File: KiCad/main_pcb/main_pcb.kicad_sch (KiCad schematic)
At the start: 11 parts

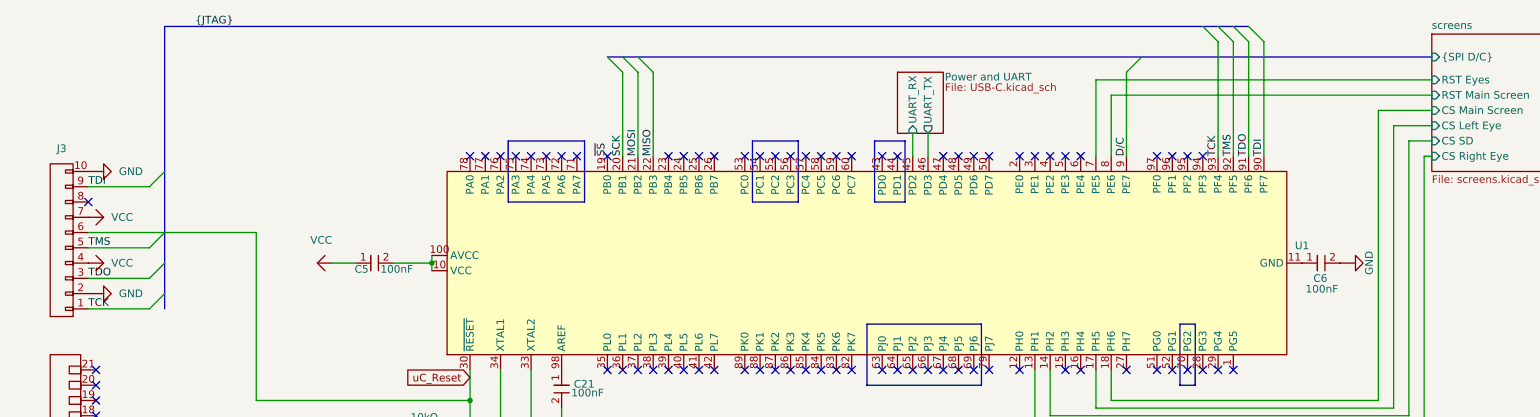
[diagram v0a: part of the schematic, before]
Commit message: feat(KiCad): Adds parallel condensators for USB-C VBUS pin
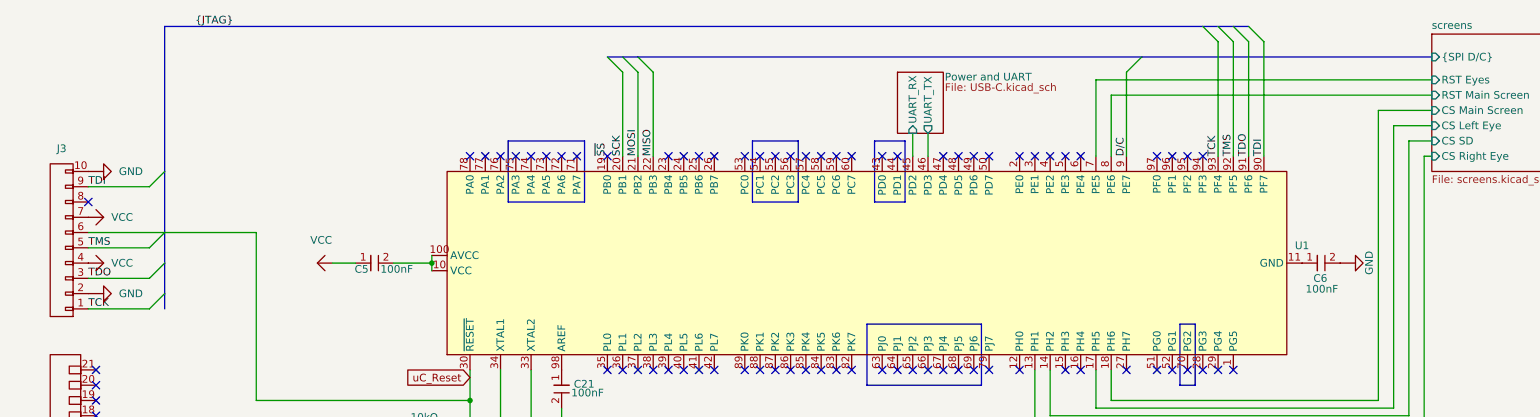
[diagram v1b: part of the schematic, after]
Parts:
- J1, J3, S2, U1, Y1: value (none) -> ~

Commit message: feat(KiCad): Fixes symbols and ERC
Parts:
- C21, C3, C4, C5, C6: symbol lilys_pad:Capacitor -> Lily's Pad:Capacitor
- J1: symbol lilys_pad:Header_21 -> Lily's Pad:Header_21
- J3: symbol lilys_pad:2X5_Header -> Lily's Pad:2X5_Header
- R1: symbol lilys_pad:Resistor -> Lily's Pad:Resistor
- S2: symbol lilys_pad:Push-button_Switch -> Lily's Pad:Push-button_Switch
- U1: symbol lilys_pad:ATmega_2560 -> Lily's Pad:ATmega_2560
- Y1: symbol lilys_pad:Crystal -> Lily's Pad:Crystal
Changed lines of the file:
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@@
 		(company "Lily's Pad")
 	)
+	(bus_alias "JTAG"
+		(members "TDI" "TMS" "TDO" "TCK")
+	)
+	(bus_alias "SPI"
+		(members "SCK" "MOSI" "MISO")
+	)
 	(rectangle
 		(start 96.52 40.6401)
@@
 	(wire
 		(pts
+			(xy 16.51 190.5) (xy 16.51 191.77)
+		)
+		(stroke
+			(width 0)
+			(type default)
+		)
+	)
+	(wire
+		(pts
 			(xy 246.38 86.36) (xy 186.69 86.36)
 		)
@@
 		)
 	)
+	(label "{SPI D{slash}C}"
+		(at 137.16 26.67 0)
+		(effects
+			(font
+				(size 1.27 1.27)
+			)
+			(justify left bottom)
+		)
+	)
 	(label "TMS"
 		(at 217.17 43.18 90)
@@
 	)
 	(symbol
-		(lib_id "lilys_pad:Capacitor")
+		(lib_id "Lily's Pad:Capacitor")
 		(at 232.41 60.96 90)
 		(unit 1)
@@
 	)
 	(symbol
-		(lib_id "lilys_pad:Capacitor")
+		(lib_id "Lily's Pad:Capacitor")
 		(at 100.33 101.6 0)
 		(unit 1)
@@
 	)
 	(symbol
-		(lib_id "lilys_pad:2X5_Header")
+		(lib_id "Lily's Pad:2X5_Header")
 		(at 22.86 57.15 180)
 		(unit 1)
@@
 		(fields_autoplaced yes)
 		(property "Reference" "J3"
-			(at 22.225 41.91 0)
+			(at 22.225 39.37 0)
 			(effects
 				(font
@@
 		)
 		(property "Value" "~"
-			(at 22.86 57.15 0)
+			(at 22.225 41.91 0)
 			(effects
 				(font
@@
 	)
 	(symbol
-		(lib_id "lilys_pad:PWR_FLG")
+		(lib_id "Lily's Pad:PWR_FLG")
 		(at 22.86 194.31 0)
 		(unit 1)
@@
 	)
 	(symbol
-		(lib_id "lilys_pad:VCC")
+		(lib_id "Lily's Pad:VCC")
 		(at 29.21 60.96 90)
 		(unit 1)
@@
 	)
 	(symbol
-		(lib_id "lilys_pad:GND")
+		(lib_id "Lily's Pad:GND")
 		(at 29.21 45.72 90)
 		(unit 1)
@@
 	)
 	(symbol
-		(lib_id "lilys_pad:Resistor")
+		(lib_id "Lily's Pad:Resistor")
 		(at 82.55 88.9 90)
 		(unit 1)
@@
 	)
 	(symbol
-		(lib_id "lilys_pad:VCC")
+		(lib_id "Lily's Pad:VCC")
 		(at 29.21 53.34 90)
 		(unit 1)
@@
 	)
 	(symbol
-		(lib_id "lilys_pad:Capacitor")
+		(lib_id "Lily's Pad:Capacitor")
 		(at 74.93 60.96 90)
 		(unit 1)
@@
 	)
 	(symbol
-		(lib_id "lilys_pad:Crystal")
+		(lib_id "Lily's Pad:Crystal")
 		(at 95.25 100.33 0)
 		(unit 1)
@@
 	)
 	(symbol
-		(lib_id "lilys_pad:VCC")
+		(lib_id "Lily's Pad:VCC")
 		(at 74.93 88.9 270)
 		(unit 1)
@@
 	)
 	(symbol
-		(lib_id "lilys_pad:Push-button_Switch")
+		(lib_id "Lily's Pad:Push-button_Switch")
 		(at 82.55 95.25 270)
 		(unit 1)
@@
 	)
 	(symbol
-		(lib_id "lilys_pad:GND")
+		(lib_id "Lily's Pad:GND")
 		(at 72.39 95.25 270)
 		(unit 1)
@@
 	)
 	(symbol
-		(lib_id "lilys_pad:ATmega_2560")
+		(lib_id "Lily's Pad:ATmega_2560")
 		(at 156.21 60.96 90)
 		(unit 1)
@@
 		(fields_autoplaced yes)
 		(property "Reference" "U1"
-			(at 228.6 58.0546 90)
+			(at 228.6 55.5146 90)
 			(effects
 				(font
@@
 		)
 		(property "Value" "~"
-			(at 156.21 60.96 0)
+			(at 228.6 58.0546 90)
 			(effects
 				(font
@@
 	)
 	(symbol
-		(lib_id "lilys_pad:GND")
+		(lib_id "Lily's Pad:GND")
 		(at 22.86 189.23 180)
 		(unit 1)
@@
 	)
 	(symbol
-		(lib_id "lilys_pad:Capacitor")
+		(lib_id "Lily's Pad:Capacitor")
 		(at 95.25 92.71 0)
 		(unit 1)
@@
 	)
 	(symbol
-		(lib_id "lilys_pad:VCC")
-		(at 16.51 189.23 180)
+		(lib_id "Lily's Pad:VCC")
+		(at 16.51 187.96 180)
 		(unit 1)
 		(exclude_from_sim no)
@@
 		(dnp no)
 		(property "Reference" "#PWR07"
-			(at 16.51 187.96 0)
+			(at 16.51 186.69 0)
 			(effects
 				(font
@@
 		)
 		(property "Value" "VCC"
-			(at 14.732 188.214 0)
+			(at 14.732 186.944 0)
 			(effects
 				(font
@@
 		)
 		(property "Footprint" ""
-			(at 16.51 189.23 0)
+			(at 16.51 187.96 0)
 			(effects
 				(font
@@
 		)
 		(property "Datasheet" ""
-			(at 16.51 189.23 0)
+			(at 16.51 187.96 0)
 			(effects
 				(font
@@
 		)
 		(property "Description" ""
-			(at 16.51 189.23 0)
+			(at 16.51 187.96 0)
 			(effects
 				(font
@@
 	)
 	(symbol
-		(lib_id "lilys_pad:Capacitor")
+		(lib_id "Lily's Pad:Capacitor")
 		(at 105.41 82.55 0)
 		(unit 1)
@@
 	)
 	(symbol
-		(lib_id "lilys_pad:GND")
+		(lib_id "Lily's Pad:GND")
 		(at 29.21 66.04 90)
 		(unit 1)
@@
 	)
 	(symbol
-		(lib_id "lilys_pad:GND")
+		(lib_id "Lily's Pad:GND")
 		(at 105.41 91.44 0)
 		(unit 1)
@@
 		)
 		(property "Value" "GND"
-			(at 107.95 92.0749 0)
+			(at 105.41 95.25 0)
 			(effects
 				(font
 					(size 1.27 1.27)
 				)
-				(justify left)
 			)
 		)
@@
 	)
 	(symbol
-		(lib_id "lilys_pad:PWR_FLG")
+		(lib_id "Lily's Pad:PWR_FLG")
 		(at 29.21 194.31 0)
 		(unit 1)
@@
 	)
 	(symbol
-		(lib_id "lilys_pad:GND")
+		(lib_id "Lily's Pad:GND")
 		(at 237.49 60.96 90)
 		(unit 1)
@@
 	)
 	(symbol
-		(lib_id "lilys_pad:Header_21")
+		(lib_id "Lily's Pad:Header_21")
 		(at 22.86 104.14 180)
 		(unit 1)
@@
 	)
 	(symbol
-		(lib_id "lilys_pad:PWR_FLG")
+		(lib_id "Lily's Pad:PWR_FLG")
 		(at 16.51 194.31 0)
 		(unit 1)
@@
 	)
 	(symbol
-		(lib_id "lilys_pad:VCC")
+		(lib_id "Lily's Pad:VCC")
 		(at 64.77 60.96 270)
 		(unit 1)
@@
 		)
 		(property "Value" "VCC"
-			(at 65.405 57.15 90)
+			(at 63.5 60.9599 90)
 			(effects
 				(font
 					(size 1.27 1.27)
 				)
+				(justify right)
 			)
 		)

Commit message: feat(KiCad): Adds SPI header for bootloader flashing
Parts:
- added J4: 2X4 Header, symbol Lily's Pad:2x4 Header
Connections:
- net MISO: now also J4.3
- net MOSI: now also J4.2
- net SCK: now also J4.1
- new net SS: J4.4
- no-connect marks 92 -> 96
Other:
- moved on the sheet: C21, C3, C4, C5, C6, J1, J3, R1, S2, U1, Y1

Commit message: feat(KiCad): Fixes SS bus alias
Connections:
- net ~{SS} is gone; now on net SS: U1.19 (PB0)
- no-connect marks 96 -> 95

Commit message: sauvegarde
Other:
- note added: "C1"
- note added: "C10"
- note added: "C2"
- note added: "C3"
- note added: "C4"
- note added: "C5"
- note added: "C6"
- note added: "C7"
- note added: "C8"
- note added: "C9"
- note added: "GND"
- note added: "R1"
- note added: "R2"
- note added: "R3"
- note added: "R4"
- note added: "SCL"
- note added: "SDA"
- note added: "SLD_SW"
- note added: "VCC"
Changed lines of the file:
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@@
 		(members "TDI" "TMS" "TDO" "TCK")
+	)
+	(bus_alias "Keyboard"
+		(members)
 	)
 	(bus_alias "SPI"
@@
 	)
 	(rectangle
-		(start 212.09 109.2201)
-		(end 214.63 119.3801)
-		(stroke
-			(width 0)
-			(type default)
-		)
-		(fill
-			(type none)
+		(start 212.09 109.2199)
+		(end 214.63 119.3799)
+		(stroke
+			(width 0)
+			(type default)
+		)
+		(fill
+			(type color)
+			(color 255 0 0 1)
 		)
 	)
@@
 		)
 	)
+	(text "R2"
+		(exclude_from_sim no)
+		(at 25.908 164.846 0)
+		(effects
+			(font
+				(size 1.27 1.27)
+			)
+		)
+	)
+	(text "R1"
+		(exclude_from_sim no)
+		(at 25.908 167.386 0)
+		(effects
+			(font
+				(size 1.27 1.27)
+			)
+		)
+	)
+	(text "C6"
+		(exclude_from_sim no)
+		(at 25.908 144.526 0)
+		(effects
+			(font
+				(size 1.27 1.27)
+			)
+		)
+	)
+	(text "VCC"
+		(exclude_from_sim no)
+		(at 25.4 129.286 0)
+		(effects
+			(font
+				(size 1.27 1.27)
+			)
+		)
+	)
+	(text "C4"
+		(exclude_from_sim no)
+		(at 25.908 149.606 0)
+		(effects
+			(font
+				(size 1.27 1.27)
+			)
+		)
+	)
+	(text "C9"
+		(exclude_from_sim no)
+		(at 25.908 136.906 0)
+		(effects
+			(font
+				(size 1.27 1.27)
+			)
+		)
+	)
 	(text "NOTE: Check load capacitors values for the crystal\nC_{1}=C_{2}=2(C_{L}-C_{stray})"
 		(exclude_from_sim no)
@@
 		(effects
 			(font
+				(size 1.27 1.27)
+			)
+		)
+	)
+	(text "SLD_SW"
+		(exclude_from_sim no)
+		(at 23.622 126.746 0)
+		(effects
+			(font
+				(size 1.27 1.27)
+			)
+		)
+	)
+	(text "C3"
+		(exclude_from_sim no)
+		(at 25.908 152.146 0)
+		(effects
+			(font
+				(size 1.27 1.27)
+			)
+		)
+	)
+	(text "C10"
+		(exclude_from_sim no)
+		(at 25.4 134.366 0)
+		(effects
+			(font
+				(size 1.27 1.27)
+			)
+		)
+	)
+	(text "SLD_SW"
+		(exclude_from_sim no)
+		(at 23.622 124.206 0)
+		(effects
+			(font
+				(size 1.27 1.27)
+			)
+		)
+	)
+	(text "SDA"
+		(exclude_from_sim no)
+		(at 25.4 119.126 0)
+		(effects
+			(font
+				(size 1.27 1.27)
+			)
+		)
+	)
+	(text "SCL"
+		(exclude_from_sim no)
+		(at 25.4 116.586 0)
+		(effects
+			(font
+				(size 1.27 1.27)
+			)
+		)
+	)
+	(text "R4"
+		(exclude_from_sim no)
+		(at 25.908 159.766 0)
+		(effects
+			(font
+				(size 1.27 1.27)
+			)
+		)
+	)
+	(text "C5"
+		(exclude_from_sim no)
+		(at 25.908 147.066 0)
+		(effects
+			(font
+				(size 1.27 1.27)
+			)
+		)
+	)
+	(text "C8"
+		(exclude_from_sim no)
+		(at 25.908 139.446 0)
+		(effects
+			(font
+				(size 1.27 1.27)
+			)
+		)
+	)
+	(text "C2"
+		(exclude_from_sim no)
+		(at 25.908 154.686 0)
+		(effects
+			(font
+				(size 1.27 1.27)
+			)
+		)
+	)
+	(text "SLD_SW"
+		(exclude_from_sim no)
+		(at 23.622 121.666 0)
+		(effects
+			(font
+				(size 1.27 1.27)
+			)
+		)
+	)
+	(text "C1"
+		(exclude_from_sim no)
+		(at 25.908 157.226 0)
+		(effects
+			(font
+				(size 1.27 1.27)
+			)
+		)
+	)
+	(text "GND"
+		(exclude_from_sim no)
+		(at 25.4 131.826 0)
+		(effects
+			(font
+				(size 1.27 1.27)
+			)
+		)
+	)
+	(text "C7"
+		(exclude_from_sim no)
+		(at 25.908 141.986 0)
+		(effects
+			(font
+				(size 1.27 1.27)
+			)
+		)
+	)
+	(text "R3"
+		(exclude_from_sim no)
+		(at 25.908 162.306 0)
+		(effects
+			(font

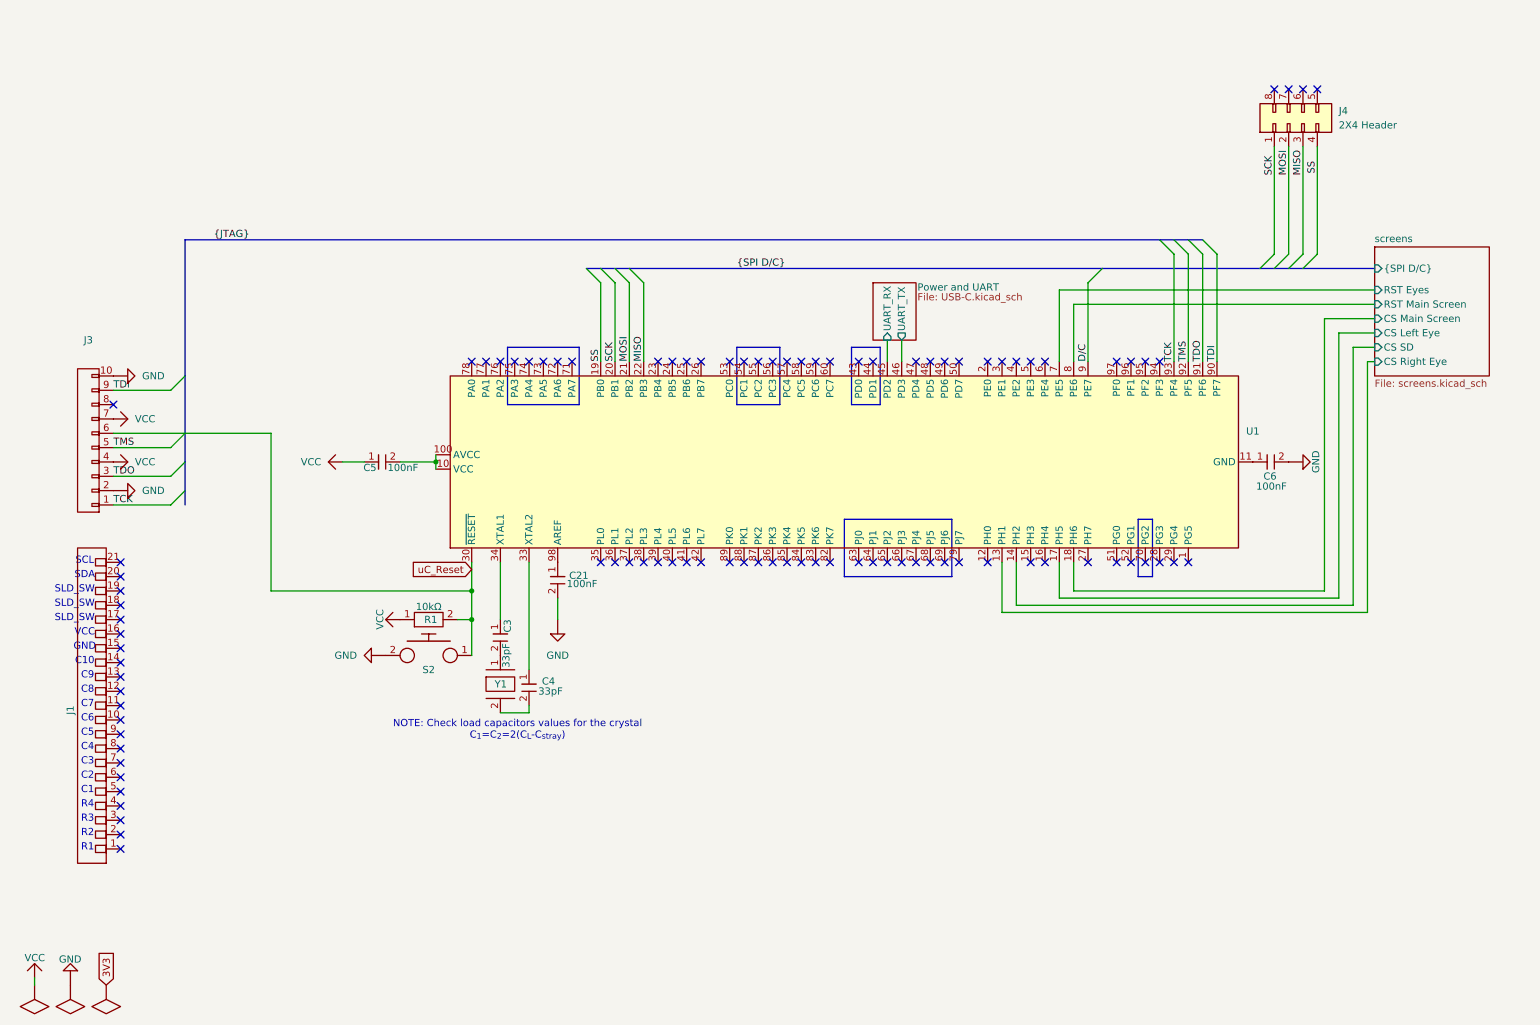
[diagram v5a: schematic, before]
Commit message: feat(KiCad): Starts addding keyboard bus
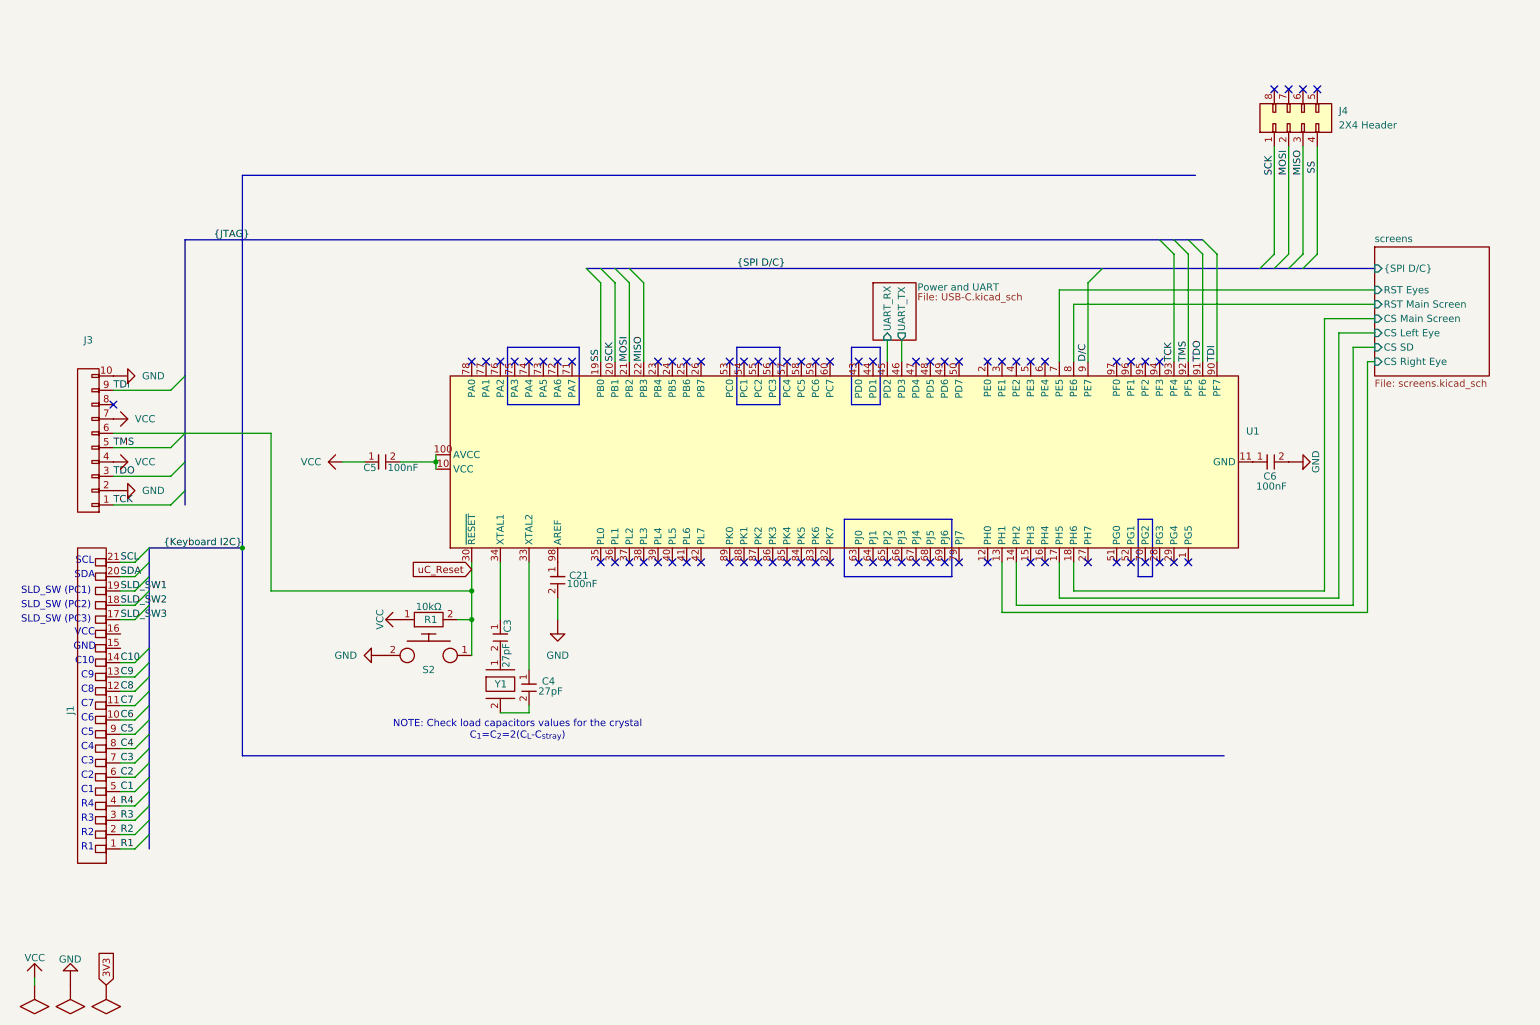
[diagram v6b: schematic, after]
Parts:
- C3, C4: value 33pF -> 27pF
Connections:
- net R1: now reaches J1.1
- net C6: now reaches J1.10
- net C7: now reaches J1.11
- net C8: now reaches J1.12
- net C9: now reaches J1.13
- net C10: now reaches J1.14
- net SLD_SW3: now reaches J1.17
- net SLD_SW2: now reaches J1.18
- net SLD_SW1: now reaches J1.19
- net R2: now reaches J1.2
- net SDA: now reaches J1.20
- net SCL: now reaches J1.21
- net R3: now reaches J1.3
- net R4: now reaches J1.4
- net C1: now reaches J1.5
- net C2: now reaches J1.6
- net C3: now reaches J1.7
- net C4: now reaches J1.8
- net C5: now reaches J1.9
- no-connect marks 95 -> 74
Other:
- note added: "SLD_SW (PC1)"
- note added: "SLD_SW (PC2)"
- note added: "SLD_SW (PC3)"
- note removed: "SLD_SW"

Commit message: feat(KiCad): Continues work
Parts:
- added D1, D2, D3, D4: ~, LED_SMD:LED_0603_1608Metric_Pad1.05x0.95mm_HandSolder, symbol Lily's Pad:LED
- added R4, R5, R6, R7: 10kΩ, Resistor_SMD:R_0201_0603Metric_Pad0.64x0.40mm_HandSolder, symbol Lily's Pad:Resistor
- C21, C3, C4, C5, C6: footprint (none) -> Capacitor_SMD:C_0201_0603Metric_Pad0.64x0.40mm_HandSolder
- R1: footprint (none) -> Resistor_SMD:R_0201_0603Metric_Pad0.64x0.40mm_HandSolder
- U1: footprint (none) -> Package_QFP:TQFP-100_14x14mm_P0.5mm
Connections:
- net C1: now also U1.75 (PA3)
- net C10: now also U1.66 (PJ3)
- net C2: now also U1.74 (PA4)
- net C3: now also U1.73 (PA5)
- net C4: now also U1.72 (PA6)
- net C5: now also U1.71 (PA7)
- net C6: now also U1.70 (PG2)
- net C7: now also U1.69 (PJ6)
- net C8: now also U1.68 (PJ5)
- net C9: now also U1.67 (PJ4)
- net GND: now also J1.15, D1.2, D2.2, D3.2, D4.2
- net MISO: now also R6.2
- net MOSI: now also R5.2
- net R1: now also U1.65 (PJ2)
- net R2: now also U1.64 (PJ1)
- net R3: now also U1.63 (PJ0)
- net R4: now also U1.60 (PC7)
- net SCK: now also R4.2
- net SCL: now also U1.43 (PD0)
- net SDA: now also U1.44 (PD1)
- net SLD_SW1: now also U1.54 (PC1)
- net SLD_SW2: now also U1.55 (PC2)
- net SLD_SW3: now also U1.56 (PC3)
- net SS: now also R7.2
- net VCC: now also J1.16
- new net: D4.1, R7.1
- new net: D2.1, R5.1
- new net: D1.1, R4.1
- new net: D3.1, R6.1
- no-connect marks 74 -> 55

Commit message: feat(KiCad): Continues work
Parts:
- J3: footprint (none) -> Connector_JST:JST_XH_B10B-XH-A_1x10_P2.50mm_Vertical
- J4: footprint (none) -> Connector_JST:JST_XH_B8B-XH-A_1x08_P2.50mm_Vertical
- S2: footprint (none) -> Button_Switch_THT:SW_PUSH-12mm
- Y1: footprint (none) -> Crystal:Crystal_SMD_ECS_CSM3X-2Pin_7.6x4.1mm
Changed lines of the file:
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@@
 			)
 		)
-		(property "Footprint" ""
+		(property "Footprint" "Connector_JST:JST_XH_B10B-XH-A_1x10_P2.50mm_Vertical"
 			(at 26.67 95.25 0)
 			(effects
@@
 			)
 		)
-		(property "Footprint" ""
+		(property "Footprint" "Crystal:Crystal_SMD_ECS_CSM3X-2Pin_7.6x4.1mm"
 			(at 99.06 138.43 0)
 			(effects
@@
 			)
 		)
-		(property "Footprint" ""
+		(property "Footprint" "Button_Switch_THT:SW_PUSH-12mm"
 			(at 86.36 133.35 0)
 			(effects
@@
 			)
 		)
-		(property "Footprint" ""
+		(property "Footprint" "Connector_JST:JST_XH_B8B-XH-A_1x08_P2.50mm_Vertical"
 			(at 240.03 38.1 0)
 			(effects
